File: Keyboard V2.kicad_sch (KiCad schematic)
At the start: 309 parts, among them J2 Conn_01x04, J3 Conn_01x02, SW1 SW_Push, SW10 SW_Push, SW11 SW_Push, SW12 SW_Push, SW13 SW_Push, SW14 SW_Push, SW15 SW_Push, SW16 SW_Push, SW17 SW_Push, SW18 SW_Push, SW19 SW_Push, SW2 SW_Push, SW20 SW_Push, SW21 SW_Push, SW22 SW_Push, SW23 SW_Push, SW24 SW_Push, SW25 SW_Push, SW26 SW_Push, SW27 SW_Push, SW28 SW_Push, SW29 SW_Push, SW3 SW_Push, SW30 SW_Push, SW31 SW_Push, SW32 SW_Push, SW33 SW_Push, SW34 SW_Push, SW35 SW_Push, SW36 SW_Push, SW37 SW_Push, SW38 SW_Push, SW39 SW_Push, SW4 SW_Push, SW40 SW_Push, SW41 SW_Push, SW42 SW_Push, SW43 SW_Push, SW44 SW_Push, SW45 SW_Push, SW46 SW_Push, SW47 SW_Push, SW48 SW_Push, SW49 SW_Push, SW5 SW_Push, SW50 SW_Push, SW51 SW_Push, SW52 SW_Push, SW53 SW_Push, SW54 SW_Push, SW55 SW_Push, SW56 SW_Push, SW57 SW_Push, SW58 SW_Push, SW59 SW_Push, SW6 SW_Push, SW60 SW_Push, SW61 SW_Push, SW62 SW_Push, SW63 SW_Push, SW64 SW_Push, SW65 SW_Push, SW66 SW_Push, SW67 SW_Push, SW68 SW_Push, SW69 SW_Push, SW7 SW_Push, SW70 SW_Push, SW71 SW_Push, SW72 SW_Push, SW73 SW_Push, SW74 SW_Push, SW75 SW_Push, SW76 SW_Push, SW77 SW_Push, SW78 SW_Push, SW79 SW_Push, SW8 SW_Push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

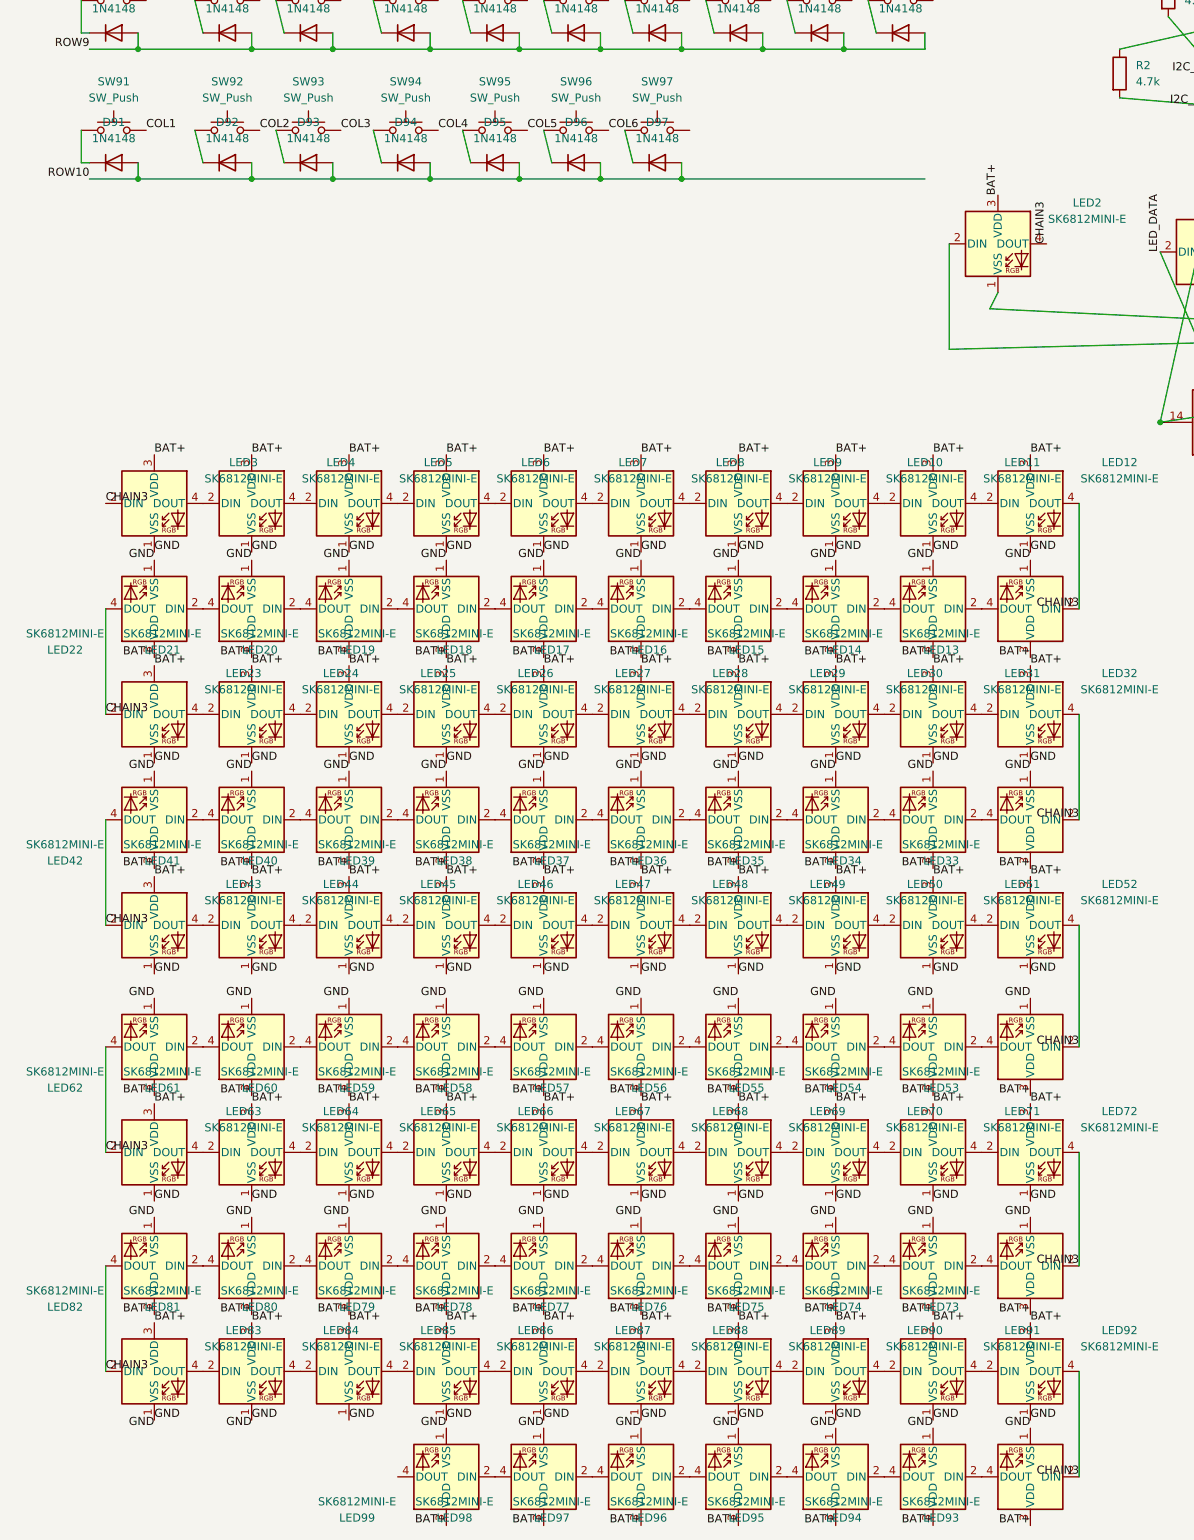
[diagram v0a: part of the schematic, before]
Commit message: Final board: nano on back, all nets routed, new gerbers/drills/STEP (2026-10-18)
Co-Authored-By: Claude Sonnet 5.5 <noreply@anthropic.com>
Claude-Session: https://claude.ai/code/session_01Mxb6JZ3vXwb4Er3iwwbvVW
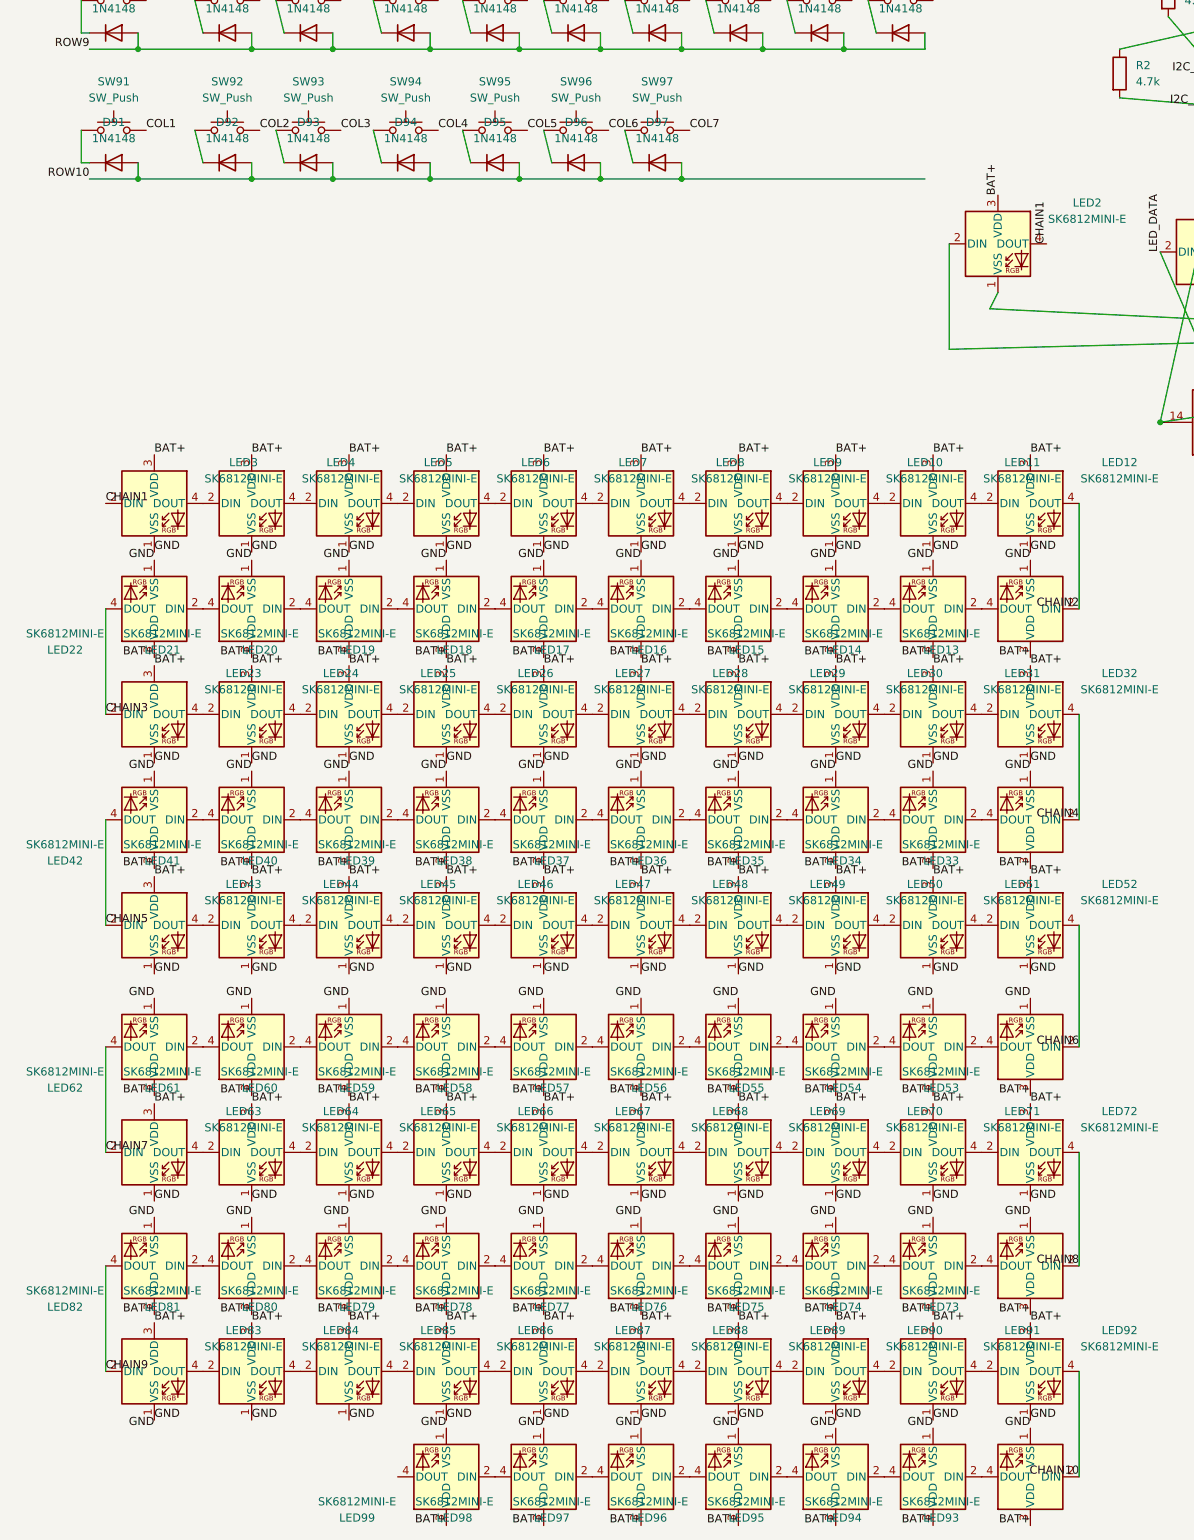
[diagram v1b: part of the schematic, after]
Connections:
- net CHAIN3: no longer LED12.4 (DOUT), LED13.2 (DIN), LED2.4 (DOUT), LED3.2 (DIN), LED32.4 (DOUT), LED33.2 (DIN), LED42.4 (DOUT), LED43.2 (DIN), LED52.4 (DOUT), LED53.2 (DIN), LED62.4 (DOUT), LED63.2 (DIN), LED72.4 (DOUT), LED73.2 (DIN), LED82.4 (DOUT), LED83.2 (DIN), LED92.4 (DOUT), LED93.2 (DIN)
- net COL7: now also SW97.2
- new net CHAIN1: LED2.4 (DOUT), LED3.2 (DIN)
- new net CHAIN10: LED92.4 (DOUT), LED93.2 (DIN)
- new net CHAIN2: LED12.4 (DOUT), LED13.2 (DIN)
- new net CHAIN4: LED32.4 (DOUT), LED33.2 (DIN)
- new net CHAIN5: LED42.4 (DOUT), LED43.2 (DIN)
- new net CHAIN6: LED52.4 (DOUT), LED53.2 (DIN)
- new net CHAIN7: LED62.4 (DOUT), LED63.2 (DIN)
- new net CHAIN8: LED72.4 (DOUT), LED73.2 (DIN)
- new net CHAIN9: LED82.4 (DOUT), LED83.2 (DIN)
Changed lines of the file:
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@@
 		)
 	)
-	(label "CHAIN3"
+	(label "CHAIN2"
 		(at 228.6 222.25 180)
 		(effects
@@
 		)
 	)
-	(label "CHAIN3"
+	(label "CHAIN7"
 		(at 76.2 307.34 0)
 		(effects
@@
 		)
 	)
-	(label "CHAIN3"
+	(label "CHAIN1"
 		(at 76.2 205.74 0)
 		(effects
@@
 		)
 	)
-	(label "CHAIN3"
+	(label "CHAIN6"
 		(at 228.6 290.83 180)
 		(effects
@@
 		)
 	)
+		(label "COL7"
+		(at 167.64 147.32 0)
+		(effects
+			(font
+				(size 1.27 1.27)
+			)
+			(justify left bottom)
+		)
+	)
 	(label "BAT+"
 		(at 205.74 262.89 180)
@@
 		)
 	)
-	(label "CHAIN3"
+	(label "CHAIN9"
 		(at 76.2 341.63 0)
 		(effects
@@
 		)
 	)
-	(label "CHAIN3"
+	(label "CHAIN8"
 		(at 228.6 325.12 180)
 		(effects
@@
 		)
 	)
-	(label "CHAIN3"
+	(label "CHAIN5"
 		(at 76.2 271.78 0)
 		(effects
@@
 		)
 	)
-	(label "GND"
-		(at 99.06 350.52 180)
-		(effects
-			(font
-				(size 1.27 1.27)
-			)
-			(justify right bottom)
-		)
-	)
 	(label "BAT+"
 		(at 114.3 334.01 0)
@@
 		)
 	)
-	(label "CHAIN3"
+	(label "CHAIN4"
 		(at 228.6 255.27 180)
 		(effects
@@
 		)
 	)
-	(label "CHAIN3"
+	(label "CHAIN10"
 		(at 228.6 358.14 180)
 		(effects
@@
 		)
 	)
-	(label "CHAIN3"
+	(label "CHAIN1"
 		(at 223.52 165.1 90)
 		(effects
